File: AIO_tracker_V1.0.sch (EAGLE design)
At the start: 52 parts, among them IC1 TPS61201, IC2 TPS61201, J1 AVR_SPI_PRG_6PTH, Q1 MOSFET-PCHANNELSMD, U1 ATMEGA328P-AU, U2 USD-SOCKETNEW

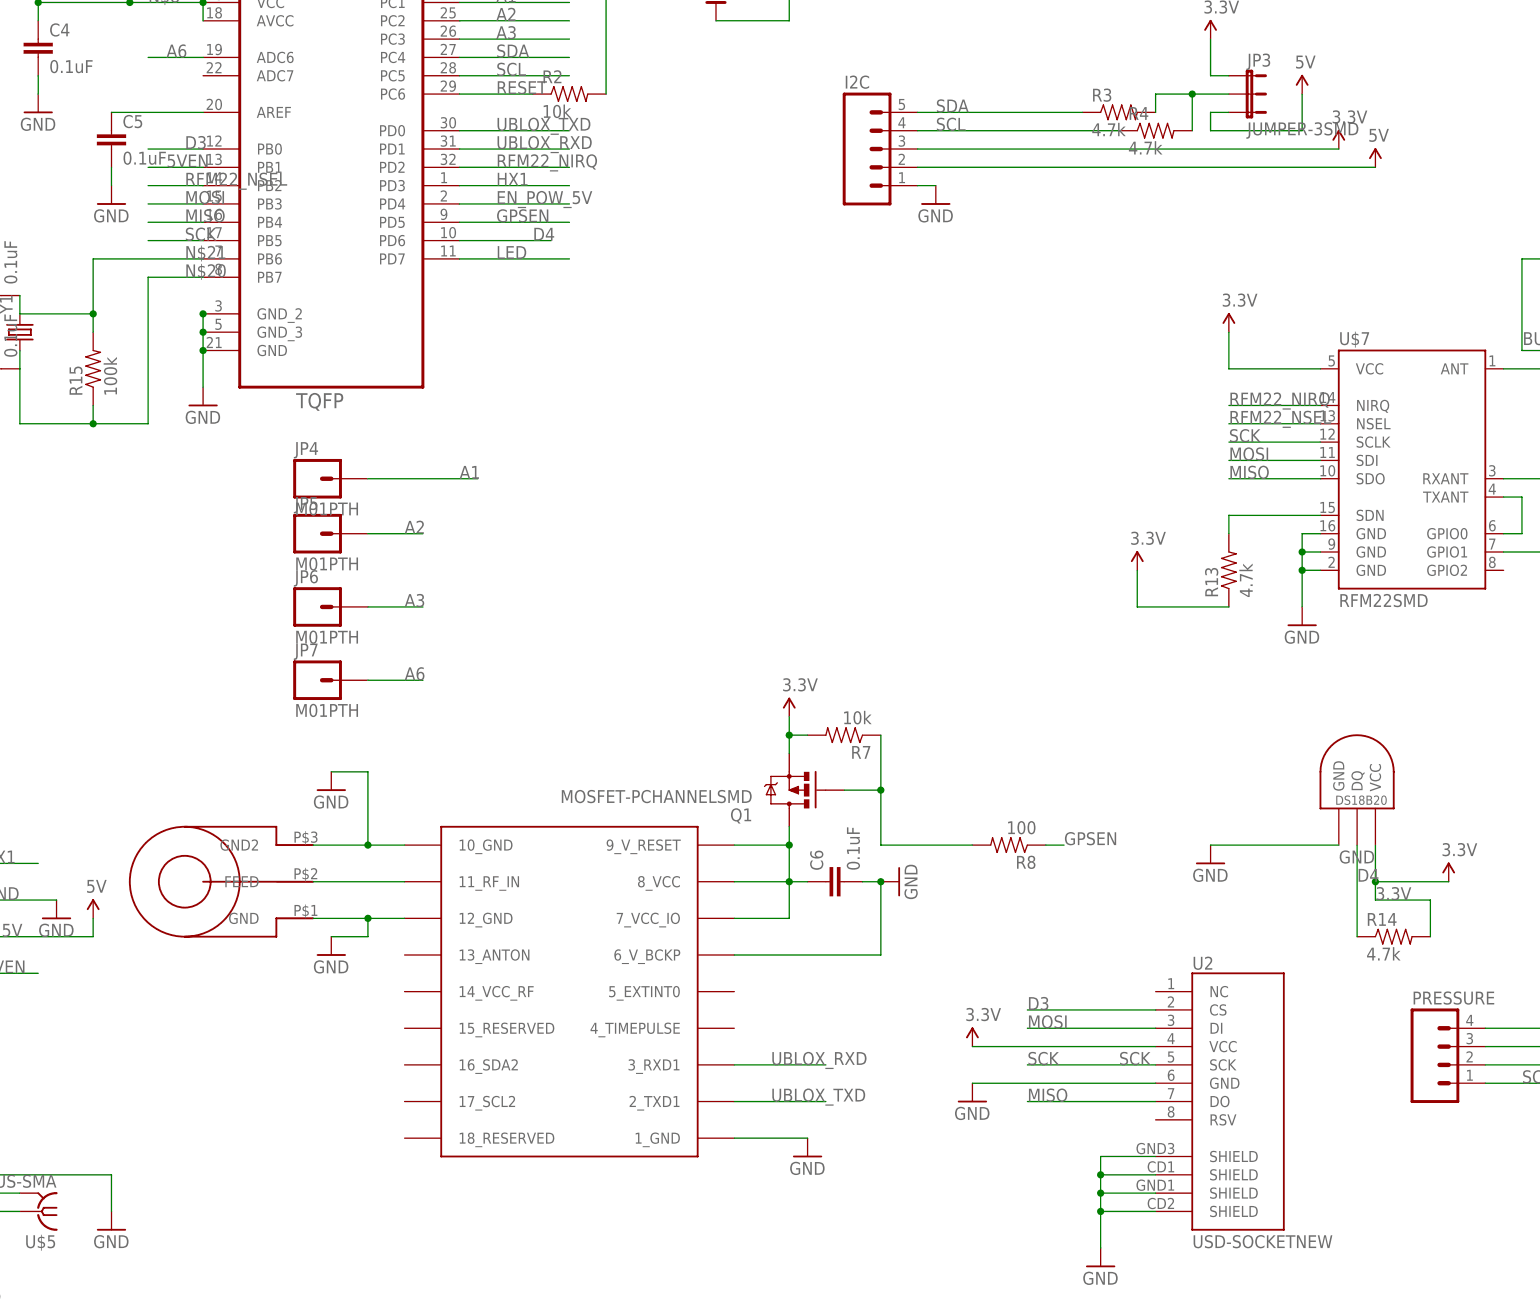
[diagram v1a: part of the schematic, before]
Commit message: Added extra power pins (5V, 3.3V and GND) and more
Added extra power pins (5V, 3.3V and GND)
Added I2C to Ublox
Placed smd jumpers in both I2C and RX/TX of Ublox for hardware selection
of communication mode.
Added pins for external RX/TX communication with arduino.
PCB layout updated
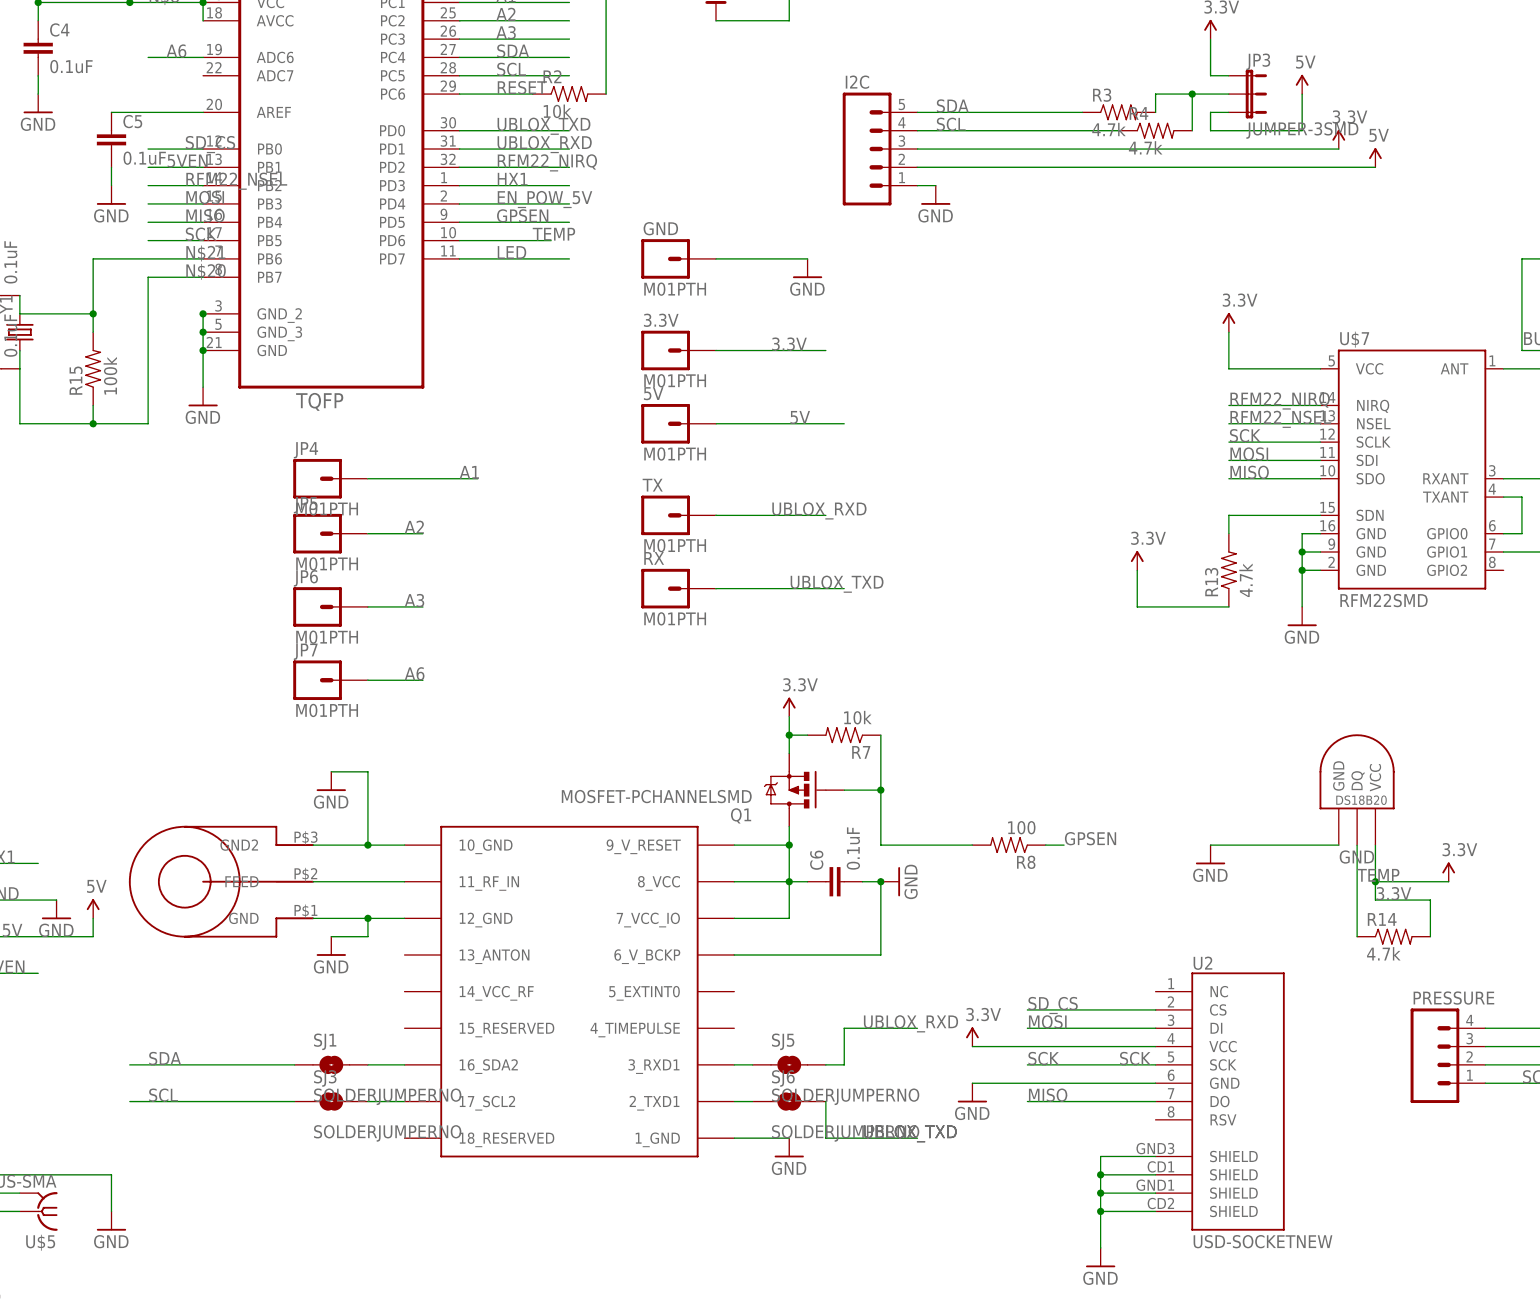
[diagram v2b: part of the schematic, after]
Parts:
- added 3.3V, 5V, GND, RX, TX: M01PTH, SparkFun-Connectors:M01PTH
- added SJ1, SJ3, SJ5, SJ6: SOLDERJUMPERNO, SparkFun-Passives:SOLDERJUMPERNO
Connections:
- net D3 renamed SD_CS
- net D4 renamed TEMP
- new net N$11: SJ5.1, U$1.3_RXD1
- new net N$12: SJ6.1, U$1.2_TXD1
- new net N$15: SJ1.2, U$1.16_SDA2
- new net N$16: SJ3.2, U$1.17_SCL2
- net 3.3V: now also 3.3V.1
- net 5V: now also 5V.1
- net GND: now also GND.1
- net SCL: now also SJ3.1
- net SDA: now also SJ1.1
- net UBLOX_RXD: now also SJ5.2, TX.1; no longer U$1.3_RXD1
- net UBLOX_TXD: now also RX.1, SJ6.2; no longer U$1.2_TXD1
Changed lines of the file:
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@@
 <part name="GND14" library="SparkFun-Aesthetics" deviceset="GND" device=""/>
 <part name="SUPPLY7" library="SparkFun-Aesthetics" deviceset="3.3V" device=""/>
-<part name="GND15" library="SparkFun-Aesthetics" deviceset="GND" device=""/>
 <part name="R7" library="SparkFun-Passives" deviceset="RESISTOR" device="0603-RES" value="10k"/>
 <part name="R8" library="SparkFun-Passives" deviceset="RESISTOR" device="0603-RES" value="100"/>
@@
 <part name="JP6" library="SparkFun-Connectors" deviceset="M01" device="PTH"/>
 <part name="JP7" library="SparkFun-Connectors" deviceset="M01" device="PTH"/>
+<part name="GND15" library="SparkFun-Aesthetics" deviceset="GND" device=""/>
+<part name="SJ5" library="SparkFun-Passives" deviceset="SOLDERJUMPER" device="NO"/>
+<part name="SJ6" library="SparkFun-Passives" deviceset="SOLDERJUMPER" device="NO"/>
+<part name="SJ1" library="SparkFun-Passives" deviceset="SOLDERJUMPER" device="NO"/>
+<part name="SJ3" library="SparkFun-Passives" deviceset="SOLDERJUMPER" device="NO"/>
+<part name="TX" library="SparkFun-Connectors" deviceset="M01" device="PTH"/>
+<part name="RX" library="SparkFun-Connectors" deviceset="M01" device="PTH"/>
+<part name="3.3V" library="SparkFun-Connectors" deviceset="M01" device="PTH"/>
+<part name="5V" library="SparkFun-Connectors" deviceset="M01" device="PTH"/>
+<part name="GND" library="SparkFun-Connectors" deviceset="M01" device="PTH"/>
+<part name="GND6" library="SparkFun-Aesthetics" deviceset="GND" device=""/>
 </parts>
 <sheets>
@@
 <instance part="GND14" gate="1" x="116.84" y="-114.3" rot="R90"/>
 <instance part="SUPPLY7" gate="G$1" x="101.6" y="-91.44"/>
-<instance part="GND15" gate="1" x="104.14" y="-152.4"/>
 <instance part="R7" gate="G$1" x="109.22" y="-93.98" rot="R180"/>
 <instance part="R8" gate="G$1" x="132.08" y="-109.22" rot="R180"/>
@@
 <instance part="JP6" gate="G$1" x="35.56" y="-76.2"/>
 <instance part="JP7" gate="G$1" x="35.56" y="-86.36"/>
+<instance part="GND15" gate="1" x="101.6" y="-152.4"/>
+<instance part="SJ5" gate="1" x="101.6" y="-139.7"/>
+<instance part="SJ6" gate="1" x="101.6" y="-144.78"/>
+<instance part="SJ1" gate="1" x="38.1" y="-139.7"/>
+<instance part="SJ3" gate="1" x="38.1" y="-144.78"/>
+<instance part="TX" gate="G$1" x="83.82" y="-63.5"/>
+<instance part="RX" gate="G$1" x="83.82" y="-73.66"/>
+<instance part="3.3V" gate="G$1" x="83.82" y="-40.64"/>
+<instance part="5V" gate="G$1" x="83.82" y="-50.8"/>
+<instance part="GND" gate="G$1" x="83.82" y="-27.94"/>
+<instance part="GND6" gate="1" x="104.14" y="-30.48"/>
 </instances>
 <busses>
@@
 <wire x1="177.8" y1="-12.7" x2="119.38" y2="-12.7" width="0.1524" layer="91"/>
 </segment>
+<segment>
+<wire x1="91.44" y1="-40.64" x2="106.68" y2="-40.64" width="0.1524" layer="91"/>
+<pinref part="3.3V" gate="G$1" pin="1"/>
+<label x="99.06" y="-40.64" size="1.778" layer="95"/>
+</segment>
 </net>
 <net name="MOSI" class="0">
@@
 <pinref part="GND11" gate="1" pin="GND"/>
 <wire x1="-10.16" y1="-165.1" x2="-10.16" y2="-167.64" width="0.1524" layer="91"/>
-</segment>
-<segment>
-<pinref part="GND15" gate="1" pin="GND"/>
-<pinref part="U$1" gate="G$1" pin="1_GND"/>
-<wire x1="104.14" y1="-149.86" x2="93.98" y2="-149.86" width="0.1524" layer="91"/>
 </segment>
 <segment>
@@
 <wire x1="121.92" y1="-17.78" x2="119.38" y2="-17.78" width="0.1524" layer="91"/>
 </segment>
+<segment>
+<pinref part="U$1" gate="G$1" pin="1_GND"/>
+<pinref part="GND15" gate="1" pin="GND"/>
+<wire x1="93.98" y1="-149.86" x2="101.6" y2="-149.86" width="0.1524" layer="91"/>
+</segment>
+<segment>
+<pinref part="GND" gate="G$1" pin="1"/>
+<wire x1="91.44" y1="-27.94" x2="104.14" y2="-27.94" width="0.1524" layer="91"/>
+<pinref part="GND6" gate="1" pin="GND"/>
+</segment>
 </net>
 <net name="N$4" class="0">
@@
 <label x="205.74" y="-139.7" size="1.778" layer="95"/>
 </segment>
+<segment>
+<wire x1="33.02" y1="-139.7" x2="10.16" y2="-139.7" width="0.1524" layer="91"/>
+<label x="12.7" y="-139.7" size="1.778" layer="95"/>
+<pinref part="SJ1" gate="1" pin="1"/>
+</segment>
 </net>
 <net name="SCL" class="0">
@@
 <label x="203.2" y="-142.24" size="1.778" layer="95"/>
 </segment>
+<segment>
+<wire x1="33.02" y1="-144.78" x2="10.16" y2="-144.78" width="0.1524" layer="91"/>
+<label x="12.7" y="-144.78" size="1.778" layer="95"/>
+<pinref part="SJ3" gate="1" pin="1"/>
+</segment>
 </net>
 <net name="UBLOX_TXD" class="0">
@@
 </segment>
 <segment>
-<pinref part="U$1" gate="G$1" pin="2_TXD1"/>
-<wire x1="93.98" y1="-144.78" x2="106.68" y2="-144.78" width="0.1524" layer="91"/>
-<label x="99.06" y="-144.78" size="1.778" layer="95"/>
+<wire x1="106.68" y1="-149.86" x2="119.38" y2="-149.86" width="0.1524" layer="91"/>
+<label x="111.76" y="-149.86" size="1.778" layer="95"/>
+<label x="111.76" y="-149.86" size="1.778" layer="95"/>
+<pinref part="SJ6" gate="1" pin="2"/>
+<wire x1="106.68" y1="-149.86" x2="106.68" y2="-144.78" width="0.1524" layer="91"/>
+</segment>
+<segment>
+<wire x1="91.44" y1="-73.66" x2="109.22" y2="-73.66" width="0.1524" layer="91"/>
+<pinref part="RX" gate="G$1" pin="1"/>
+<label x="101.6" y="-73.66" size="1.778" layer="95"/>
 </segment>
 </net>
@@
 </segment>
 <segment>
-<pinref part="U$1" gate="G$1" pin="3_RXD1"/>
-<wire x1="93.98" y1="-139.7" x2="106.68" y2="-139.7" width="0.1524" layer="91"/>
-<label x="99.06" y="-139.7" size="1.778" layer="95"/>
+<label x="111.76" y="-134.62" size="1.778" layer="95"/>
+<pinref part="SJ5" gate="1" pin="2"/>
+<wire x1="109.22" y1="-134.62" x2="119.38" y2="-134.62" width="0.1524" layer="91"/>
+<wire x1="106.68" y1="-139.7" x2="109.22" y2="-139.7" width="0.1524" layer="91"/>
+<wire x1="109.22" y1="-139.7" x2="109.22" y2="-134.62" width="0.1524" layer="91"/>
+</segment>
+<segment>
+<wire x1="91.44" y1="-63.5" x2="106.68" y2="-63.5" width="0.1524" layer="91"/>
+<pinref part="TX" gate="G$1" pin="1"/>
+<label x="99.06" y="-63.5" size="1.778" layer="95"/>
 </segment>
 </net>
@@
 <wire x1="5.08" y1="-38.1" x2="5.08" y2="-35.56" width="0.1524" layer="91"/>
 <junction x="5.08" y="-35.56"/>
-</segment>
-</net>
-<net name="D4" class="0">
-<segment>
-<pinref part="U$9" gate="G$1" pin="DQ"/>
-<wire x1="180.34" y1="-109.22" x2="180.34" y2="-121.92" width="0.1524" layer="91"/>
-<label x="180.34" y="-114.3" size="1.778" layer="95"/>
-<pinref part="R14" gate="G$1" pin="1"/>
-</segment>
-<segment>
-<pinref part="U1" gate="A" pin="PD6"/>
-<wire x1="68.58" y1="-25.4" x2="55.88" y2="-25.4" width="0.1524" layer="91"/>
-<label x="66.04" y="-25.4" size="1.778" layer="95"/>
-</segment>
-</net>
-<net name="D3" class="0">
-<segment>
-<pinref part="U1" gate="A" pin="PB0"/>
-<wire x1="20.32" y1="-12.7" x2="12.7" y2="-12.7" width="0.1524" layer="91"/>
-<label x="17.78" y="-12.7" size="1.778" layer="95"/>
-</segment>
-<segment>
-<pinref part="U2" gate="G$1" pin="CS"/>
-<wire x1="152.4" y1="-132.08" x2="134.62" y2="-132.08" width="0.1524" layer="91"/>
-<label x="134.62" y="-132.08" size="1.778" layer="95"/>
 </segment>
 </net>
@@
 <wire x1="182.88" y1="-15.24" x2="119.38" y2="-15.24" width="0.1524" layer="91"/>
 </segment>
+<segment>
+<wire x1="91.44" y1="-50.8" x2="109.22" y2="-50.8" width="0.1524" layer="91"/>
+<pinref part="5V" gate="G$1" pin="1"/>
+<label x="101.6" y="-50.8" size="1.778" layer="95"/>
+</segment>
 </net>
 <net name="N$8" class="0">
@@
 </segment>
 </net>
+<net name="N$11" class="0">
+<segment>
+<pinref part="U$1" gate="G$1" pin="3_RXD1"/>
+<pinref part="SJ5" gate="1" pin="1"/>
+<wire x1="93.98" y1="-139.7" x2="96.52" y2="-139.7" width="0.1524" layer="91"/>
+</segment>
+</net>
+<net name="N$12" class="0">
+<segment>
+<pinref part="U$1" gate="G$1" pin="2_TXD1"/>
+<pinref part="SJ6" gate="1" pin="1"/>
+<wire x1="93.98" y1="-144.78" x2="96.52" y2="-144.78" width="0.1524" layer="91"/>
+</segment>
+</net>
+<net name="N$15" class="0">
+<segment>
+<pinref part="SJ1" gate="1" pin="2"/>
+<wire x1="43.18" y1="-139.7" x2="48.26" y2="-139.7" width="0.1524" layer="91"/>
+<pinref part="U$1" gate="G$1" pin="16_SDA2"/>
+</segment>
+</net>
+<net name="N$16" class="0">
+<segment>
+<pinref part="SJ3" gate="1" pin="2"/>
+<wire x1="48.26" y1="-144.78" x2="43.18" y2="-144.78" width="0.1524" layer="91"/>
+<pinref part="U$1" gate="G$1" pin="17_SCL2"/>
+</segment>
+</net>
+<net name="SD_CS" class="0">
+<segment>
+<pinref part="U1" gate="A" pin="PB0"/>
+<wire x1="20.32" y1="-12.7" x2="12.7" y2="-12.7" width="0.1524" layer="91"/>
+<label x="17.78" y="-12.7" size="1.778" layer="95"/>
+</segment>
+<segment>
+<pinref part="U2" gate="G$1" pin="CS"/>
+<wire x1="152.4" y1="-132.08" x2="134.62" y2="-132.08" width="0.1524" layer="91"/>
+<label x="134.62" y="-132.08" size="1.778" layer="95"/>
+</segment>
+</net>
+<net name="TEMP" class="0">
+<segment>
+<pinref part="U1" gate="A" pin="PD6"/>
+<wire x1="68.58" y1="-25.4" x2="55.88" y2="-25.4" width="0.1524" layer="91"/>
+<label x="66.04" y="-25.4" size="1.778" layer="95"/>
+</segment>
+<segment>
+<pinref part="U$9" gate="G$1" pin="DQ"/>
+<wire x1="180.34" y1="-109.22" x2="180.34" y2="-121.92" width="0.1524" layer="91"/>
+<label x="180.34" y="-114.3" size="1.778" layer="95"/>
+<pinref part="R14" gate="G$1" pin="1"/>
+</segment>
+</net>
